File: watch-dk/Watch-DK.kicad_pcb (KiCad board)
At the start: 4 copper layers, 100 x 70 mm, 126 parts, among them IC401 nPM1300-QEXX, IC501 APDS-9306-065, IC502 BMI270, IC503 LIS2MDLTR, IC504 BMP581, IC505 DRV2603RUNT, IC506 PCA9306JK, IC507 RV-8263-C8, IC601 FAN5622SX, IC602 USBLC6-2P6, IC603 MX25U51245GZ4I00, IC604 NTS0104GU12, M601 NORA-B106, Q401 PMZ550UNEYL, Q402 PMZ550UNEYL, Q403 PMZ550UNEYL, Q404 PMZB320UPEYL, Q501 PMZB320UPEYL, X401 Battery, X402 Battery, X403 Power, X501 Current, X502 I2S, X503 Current, X504 I2C, X505 Current, X506 Current, X507 Current, X508 Current, X509 Motor, X510 Current, X601 DEBUG, X602 Current, X603 Device, X604 UART, X605 GPIO, X606 Current, X607 IO Current, X608 Display, X609 Touch Current, X610 LED Current

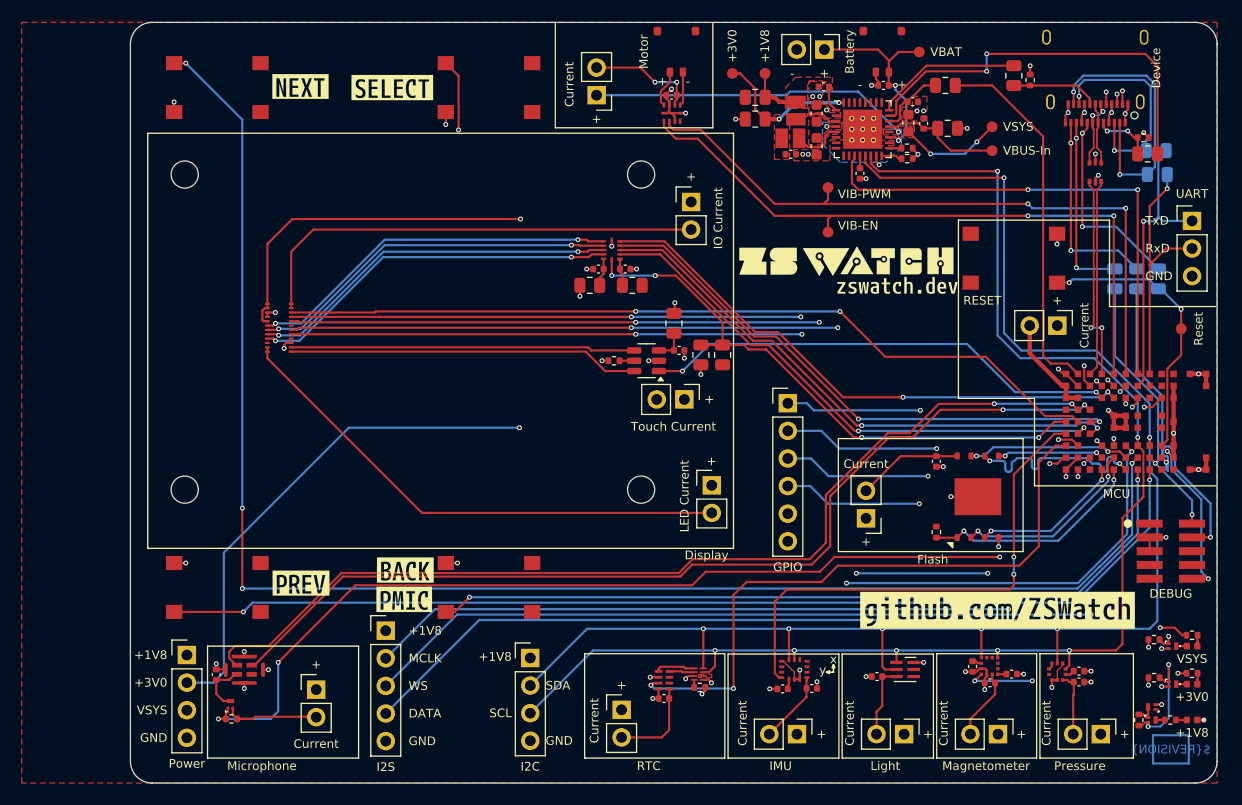
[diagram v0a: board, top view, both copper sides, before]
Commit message: Fix wrong part number for SWD connector, fix missing footprint for RTC level shifter, cosmetic changes
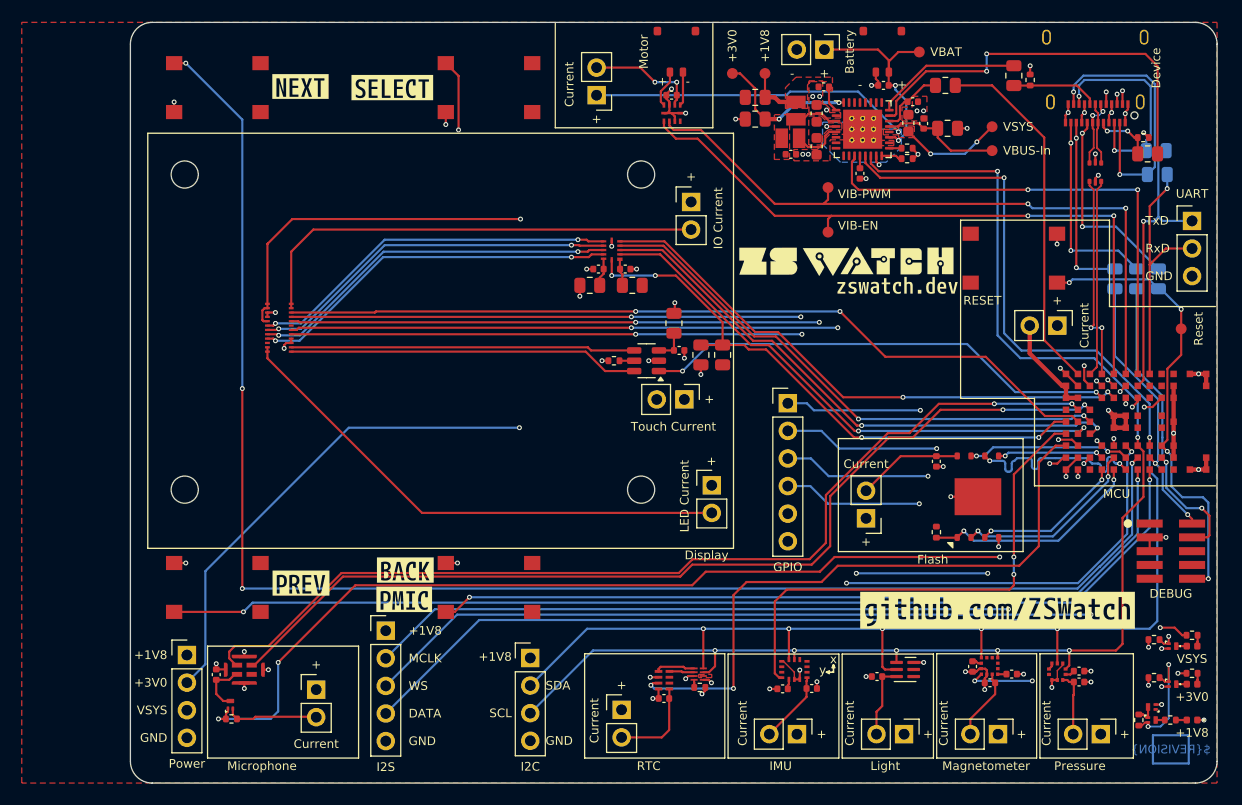
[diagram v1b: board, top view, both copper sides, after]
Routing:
- net SWDCLK: track 33.2 -> 28.6 mm
- net TOUCH-SDA: track 51.8 -> 50.2 mm
- net +3V0: track 105.6 -> 104.2 mm
- net RESETn: track 41.3 -> 42.4 mm
- net /Project Architecture/MCU/USB-VBUS-Out: track 34.1 -> 33.2 mm
